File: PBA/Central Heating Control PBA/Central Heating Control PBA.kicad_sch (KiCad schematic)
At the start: 153 parts, among them J1 Screw_Terminal_01x03, J10 Screw_Terminal_01x02, J11 Screw_Terminal_01x02, J12 Screw_Terminal_01x02, J13 Screw_Terminal_01x02, J2 Conn_01x11, J3 Screw_Terminal_01x02, J3_DC5V1 Screw_Terminal_01x02, J4 Screw_Terminal_01x02, J4_AC_OUTPUT1 Screw_Terminal_01x02, J5 Screw_Terminal_01x02, J5_AC_INPUT1 Screw_Terminal_01x02, J6 Screw_Terminal_01x02, J7 Screw_Terminal_01x02, J8 Screw_Terminal_01x02, J9 Screw_Terminal_01x02, Q1 BT136-600, Q10 BT136-600, Q11 BC857, Q12 BC857, Q13 BC857, Q14 BC857, Q15 BC857, Q16 BC857, Q17 BC857, Q18 BC857, Q19 BC857, Q2 BT136-600, Q20 BC857, Q21 BC857, Q22 BT136-600, Q3 BT136-600, Q4 BT136-600, Q5 BT136-600, Q6 BT136-600, Q7 BT136-600, Q8 BT136-600, Q9 BT136-600, U1 ESP32_DevKit_V1_DOIT, U10 MOC3083M, U11 MOC3083M, U12 MOC3083M, U2 MOC3083M, U3 MOC3083M, U4 MOC3083M, U5 MOC3083M, U6 MOC3083M, U7 MOC3083M, U8 MOC3083M, U9 MOC3083M

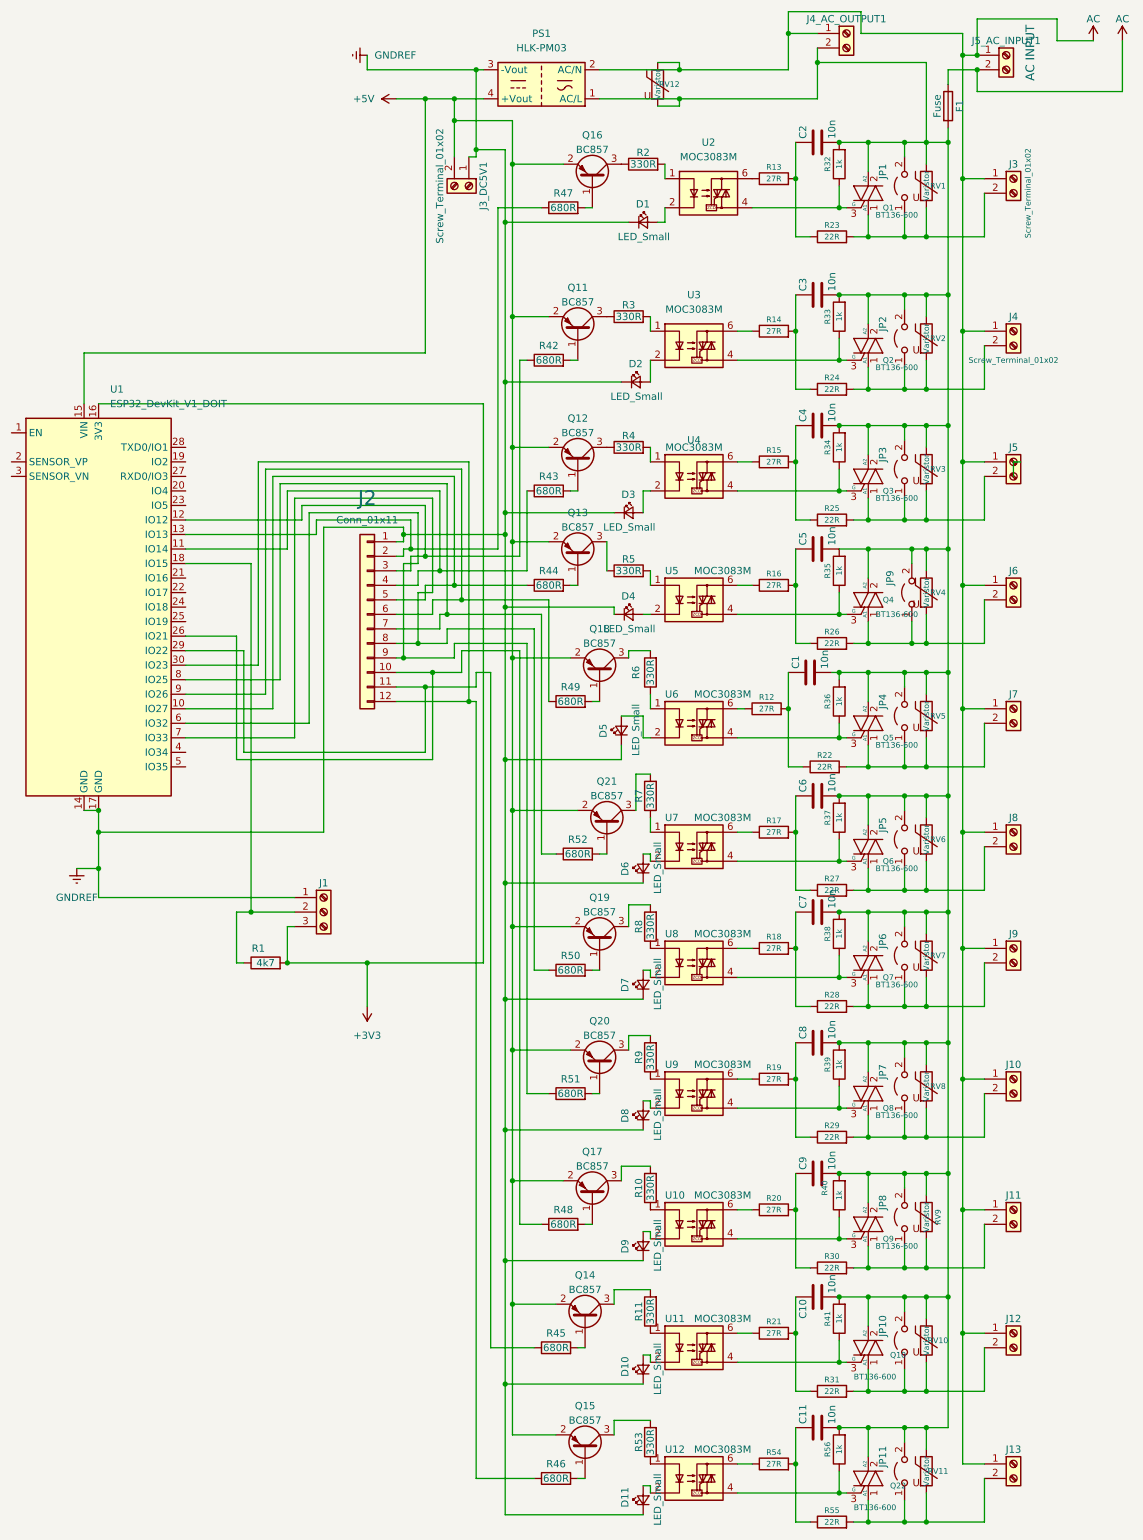
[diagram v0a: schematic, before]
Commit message: Update PBA for DHT22 and footprints... Removed ArduinoJson adding getJsonVal function recuces about 4k of code for only read json value
Signed-off-by: rgw <rgw@marm.pl>
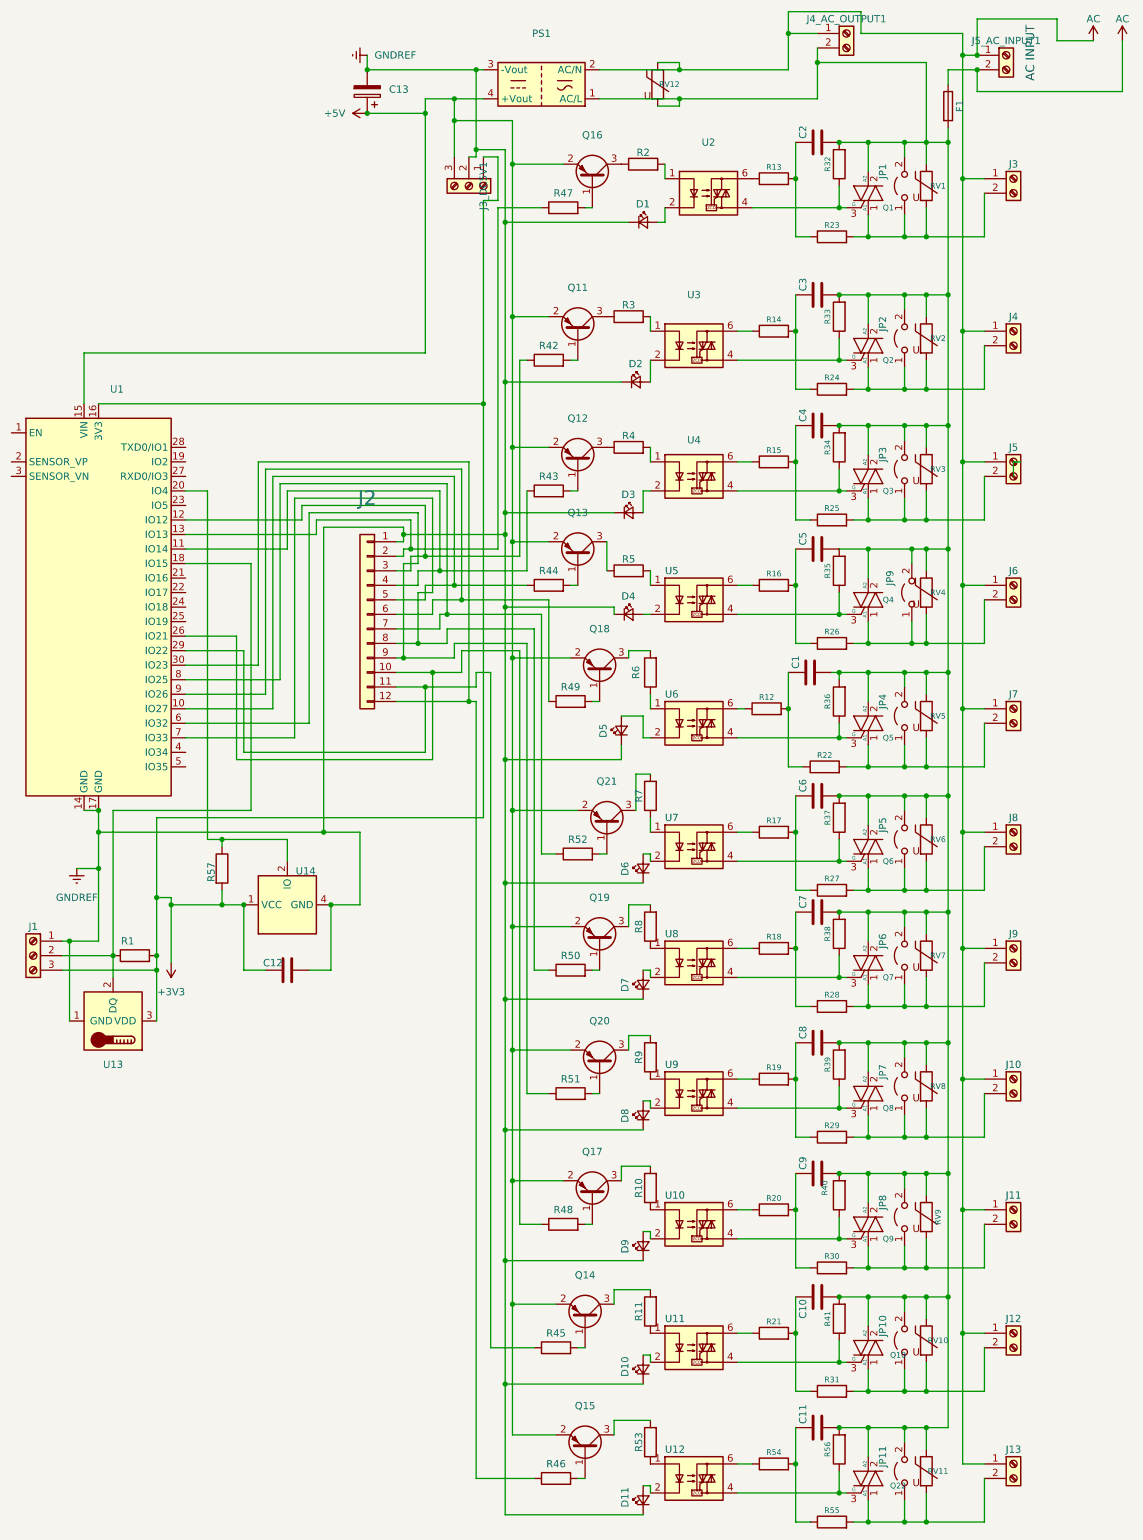
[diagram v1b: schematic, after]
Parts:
- added C12: (no value), symbol Device:C
- added C13: (no value), symbol Device:C_Polarized
- added R57: (no value), symbol Device:R
- added U13: (no value), symbol Sensor_Temperature:DS18B20
- added U14: (no value), symbol Sensor:DHT11
- C1, C10, C11, C2, C3, C4, C5, C6, C7, C8, C9: value 10n -> (none); footprint Capacitor_THT:C_Rect_L19.0mm_W7.0mm_P15.00mm_MKS4 -> (none)
- D1, D10, D11, D2, D3, D4, D5, D6, D7, D8, D9: value LED_Small -> (none); footprint LED_THT:LED_D3.0mm_Clear -> (none)
- F1: value Fuse -> (none); footprint Fuse:Fuseholder_Littelfuse_100_series_5x20mm -> (none)
- J1: value Screw_Terminal_01x03 -> (none); footprint TerminalBlock:TerminalBlock_bornier-3_P5.08mm -> (none)
- J10, J11, J12, J13, J3, J4, J4_AC_OUTPUT1, J5, J6, J7, J8, J9: value Screw_Terminal_01x02 -> (none); footprint TerminalBlock_MetzConnect:TerminalBlock_MetzConnect_Type055_RT01502HDWU_1x02_P5.00mm_Horizontal -> (none)
- J2: value Conn_01x11 -> (none); footprint Connector_PinHeader_2.54mm:PinHeader_1x12_P2.54mm_Vertical -> (none)
- J3_DC5V1: value Screw_Terminal_01x02 -> (none); footprint TerminalBlock_MetzConnect:TerminalBlock_MetzConnect_Type055_RT01502HDWU_1x02_P5.00mm_Horizontal -> (none); symbol Connector:Screw_Terminal_01x02 -> Connector:Screw_Terminal_01x03
- J5_AC_INPUT1: value Screw_Terminal_01x02 -> (none); footprint TerminalBlock:TerminalBlock_bornier-2_P5.08mm -> (none)
- JP1, JP10, JP11, JP2, JP3, JP4, JP5, JP6, JP7, JP8, JP9: value Jumper_2_Open -> (none); footprint Connector_PinSocket_2.54mm:PinSocket_1x02_P2.54mm_Vertical -> (none)
- PS1: value HLK-PM03 -> (none); footprint Converter_ACDC:Converter_ACDC_HiLink_HLK-PMxx -> (none)
- Q1, Q10, Q2, Q22, Q3, Q4, Q5, Q6, Q7, Q8, Q9: value BT136-600 -> (none); footprint Package_TO_SOT_THT:TO-220-3_Vertical -> (none)
- Q11, Q12, Q13, Q14, Q15, Q16, Q17, Q18, Q19, Q20, Q21: value BC857 -> (none); footprint Package_TO_SOT_SMD:SOT-23 -> (none)
- R1: value 4k7 -> (none); footprint Resistor_SMD:R_0805_2012Metric_Pad1.20x1.40mm_HandSolder -> (none)
- R10, R11, R2, R3, R4, R5, R53, R6, R7, R8, R9: value 330R -> (none); footprint Resistor_SMD:R_0805_2012Metric_Pad1.20x1.40mm_HandSolder -> (none)
- R12, R13, R14, R15, R16, R17, R18, R19, R20, R21, R54: value 27R -> (none); footprint Resistor_THT:R_Axial_DIN0207_L6.3mm_D2.5mm_P2.54mm_Vertical -> (none)
- R22, R23, R24, R25, R26, R27, R28, R29, R30, R31, R55: value 22R -> (none); footprint Resistor_THT:R_Axial_DIN0207_L6.3mm_D2.5mm_P2.54mm_Vertical -> (none)
- R32, R33, R34, R35, R36, R37, R38, R39, R40, R41, R56: value 1k -> (none); footprint Resistor_THT:R_Axial_DIN0207_L6.3mm_D2.5mm_P2.54mm_Vertical -> (none)
- R42, R43, R44, R45, R46, R47, R48, R49, R50, R51, R52: value 680R -> (none); footprint Resistor_SMD:R_0805_2012Metric_Pad1.20x1.40mm_HandSolder -> (none)
- RV1, RV10, RV11, RV12, RV2, RV3, RV4, RV5, RV6, RV7, RV8, RV9: value Varistor -> (none); footprint Varistor:RV_Disc_D9mm_W3.3mm_P5mm -> (none)
- U1: value ESP32_DevKit_V1_DOIT -> (none); footprint Espressif:esp32_devkit_v1_doit -> (none)
- U10, U11, U12, U2, U3, U4, U5, U6, U7, U8, U9: value MOC3083M -> (none); footprint Package_DIP:DIP-6_W7.62mm_Socket_LongPads -> (none)
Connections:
- net +3V3: now also J3_DC5V1.1 (Pin_1), C12.1, R57.2, U13.3 (VDD), U14.1 (VCC)
- net +5V: now also J3_DC5V1.3 (Pin_3), C13.1; no longer J3_DC5V1.2 (Pin_2)
- net GNDREF: now also J3_DC5V1.2 (Pin_2), C12.2, C13.2, U13.1 (GND), U14.4 (GND); no longer J3_DC5V1.1 (Pin_1)
- net at J1.2 (Pin_2), R1.1, U1.18 (IO15): now also U13.2 (DQ)
- net at U1.20 (IO4): now also R57.1, U14.2 (IO)
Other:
- moved on the sheet: J1, R1
